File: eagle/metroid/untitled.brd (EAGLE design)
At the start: 100 x 80 mm, 4 parts, among them IC1 MEGA48/88/168-AU, U1 AT45DB321D-S

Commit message: before adding humidity
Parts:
- added C1: 1uF, ng:1206
- added C2, C3, C4, C5, C6: .1uF, ng:1206
- added IC4: MIC5219BM5, metrify:SOT23-5
- added PWR: (no value), con-lstb:MA03-1
- added Q1: (no value), crystal:TC26H
- added S1: (no value), fab:6MM_SWITCH
- added SV1: (no value), con-lstb:MA04-2
- added SV2: (no value), con-lstb:MA08-1
- added U$1: BS-7BATTERYCLIP, metrify:BS-7PACKAGE
- added U$2: DS18S20, metrify:TO92
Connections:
- net N$1 renamed PORTC
- removed net +5V: WRL-00691.1
- removed net AGND: IC1.21
- new net N$1: C6.2, IC1.20
- new net N$10: IC1.27, SV2.5
- new net N$11: IC1.28, SV2.6
- new net N$12: IC1.19, SV2.7
- new net N$13: IC1.22, SV2.8
- new net N$14: IC4.1, IC4.3, PWR.3
- new net N$3: IC1.7, Q1.2
- new net N$4: IC1.8, Q1.1
- new net N$5: IC1.2, U$2.2
- new net N$6: IC1.23, S1.1, S1.2, SV2.1
- new net N$7: IC1.24, SV2.2
- new net N$8: IC1.25, SV2.3
- new net N$9: IC1.26, SV2.4
- net +3V3: now also C1.2, C2.2, C3.2, C4.2, C5.2, IC1.18, IC4.5, PWR.2, SV1.7, U$1.POS, U$2.1, WRL-00691.1
- net GND: now also C1.1, C2.1, C3.1, C4.1, C5.1, C6.1, IC1.21, IC4.2, PWR.1, S1.3, S1.4, SV1.8, U$1.NEG, U$2.3
- net MISO: now also SV1.2
- net MOSI: now also SV1.3
- net RFCEN: now also SV1.6
- net RFIRQ: now also SV1.1
- net RFSPICS: now also SV1.5
- net SCK: now also SV1.4

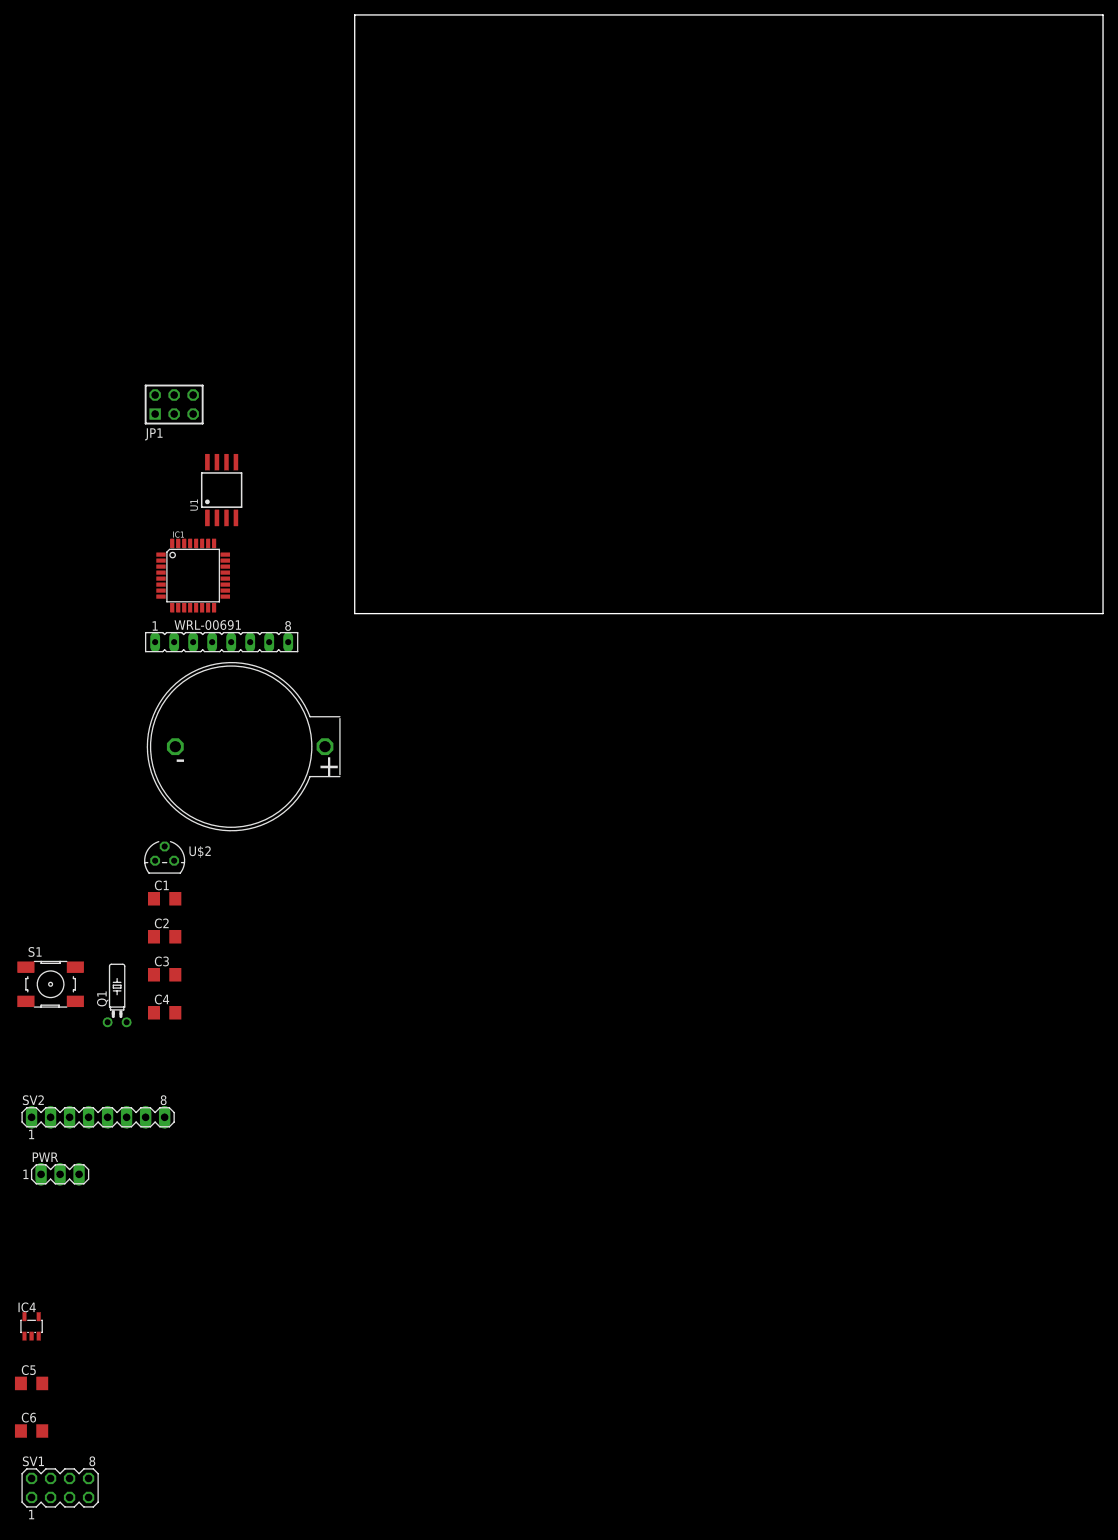
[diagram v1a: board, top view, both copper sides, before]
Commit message: board routed. eagle 6. 6 mil traces, qfp atmega+battery+labpowerheaders+headers>sparkfunnordic or mdfly+pads for 1206 sensors, humidity, phototransistor+isp+pushbutton
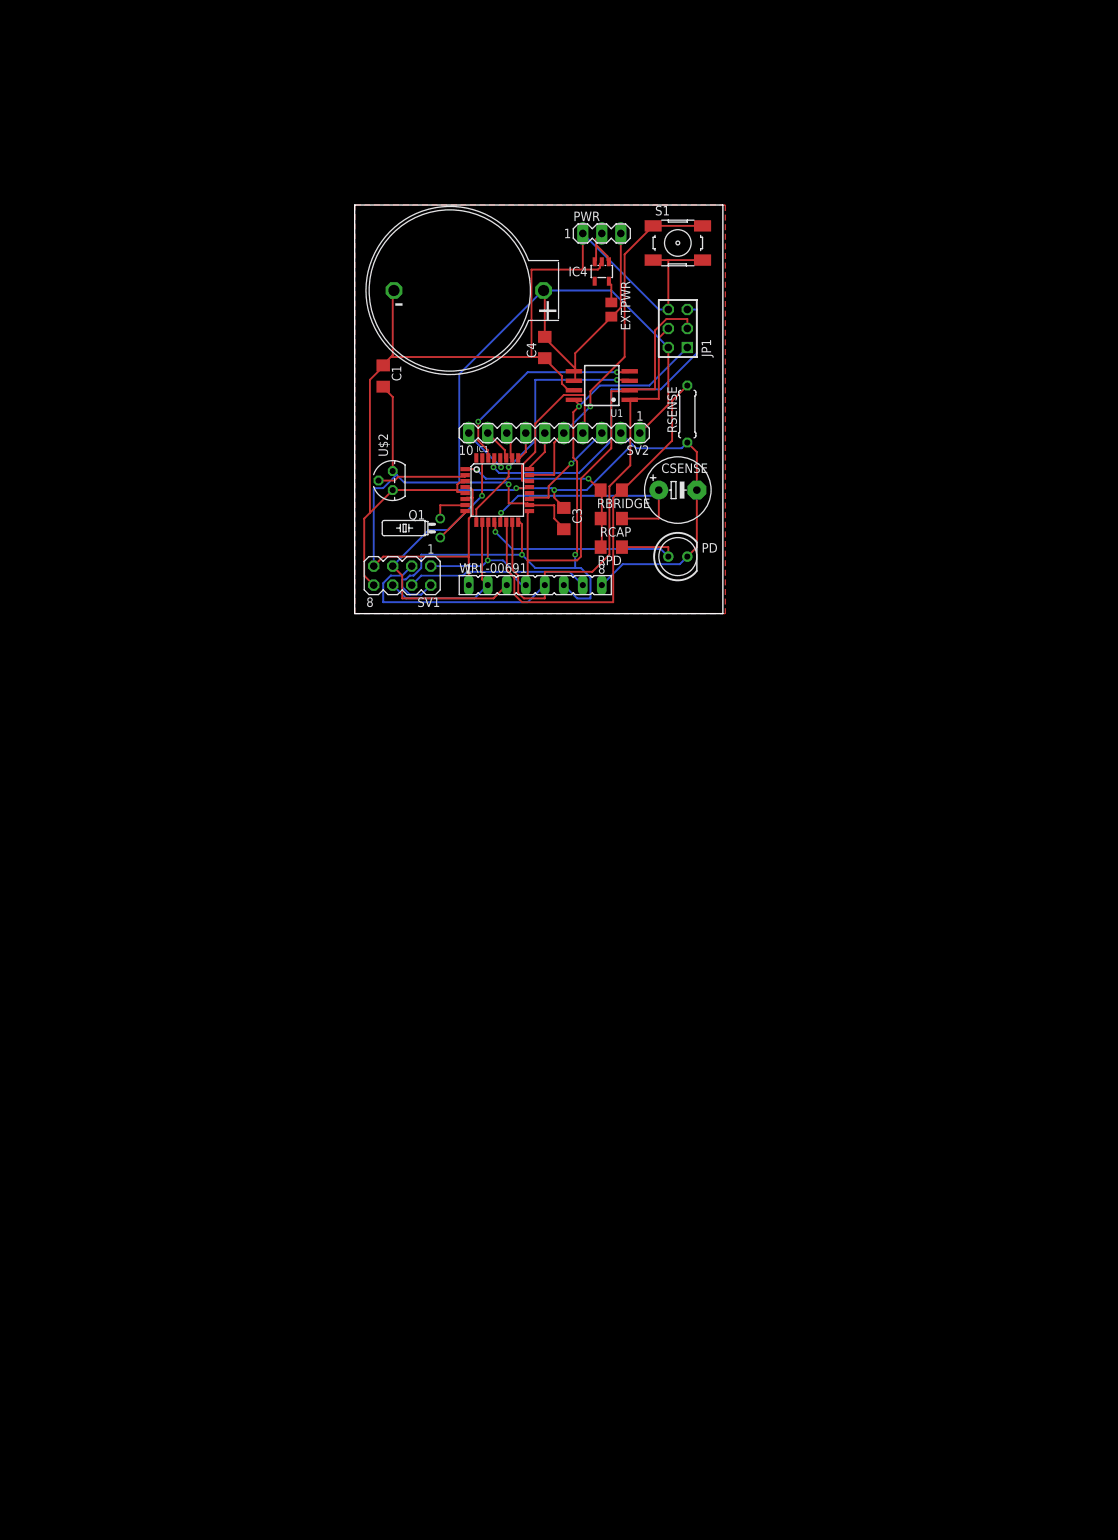
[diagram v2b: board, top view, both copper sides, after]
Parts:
- removed C2, C5, C6: .1uF, ng:1206
- added CSENSE: (no value), rcl:E5-8,5
- added EXTPWR: (no value), rcl:M0805
- added PD: (no value), ng:5MM
- added RBRIDGE, RCAP, RPD: (no value), ng:1206
- added RSENSE: (no value), rcl:0207/7
- JP1: value AVR-ISP-6VERT -> AVR-ISP
- SV1: value (none) -> RF-IS2411
- SV2: value (none) -> ADC; device con-lstb:MA08-1 -> con-lstb:MA10-1
- moved IC4 160.2 mm to (33.0, 45.7), turned to 180 degrees
- moved PWR 145.1 mm to (33.0, 50.8)
- moved SV1 130.2 mm to (6.35, 5.08), turned to 180 degrees
- moved S1 129.8 mm to (43.2, 49.5)
- moved SV2 109.9 mm to (26.7, 24.1), turned to 180 degrees
- moved C4 102.4 mm to (25.4, 35.6), turned to 90 degrees
- moved C3 81.0 mm to (27.9, 12.7), turned to 270 degrees
- moved Q1 78.9 mm to (11.4, 11.4), turned to 90 degrees
- moved C1 75.7 mm to (3.81, 31.8), turned to 270 degrees
- moved JP1 68.1 mm to (43.2, 38.1), turned to 90 degrees
- moved U$1 67.6 mm to (15.2, 43.2)
- moved U$2 59.2 mm to (5.08, 17.8), turned to 90 degrees
- moved U1 52.7 mm to (33.0, 30.5), turned to 90 degrees
- moved WRL-00691 42.6 mm to (24.1, 3.81)
- moved IC1 42.2 mm to (19.1, 16.5)
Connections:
- net N$5 renamed 1WIRE
- removed net N$1: C6.2, IC1.20
- removed net N$7: IC1.24, SV2.2
- new net AUXSENSE: IC1.1, RBRIDGE.2, RCAP.2, RPD.2
- new net HUMIDITY: CSENSE.+, IC1.13, RCAP.1
- new net N$15: IC1.19, SV2.3
- new net N$5: EXTPWR.1, IC4.5
- new net PHOTODIODE: IC1.12, PD.IN, RPD.1
- new net RBRIDGE: IC1.14, RBRIDGE.1, RSENSE.2
- net +3V3: now also EXTPWR.2, PWR.3, SV2.1; no longer C2.2, C5.2, IC4.5, PWR.2
- net GND: now also CSENSE.-, PD.OUT, RSENSE.1, SV2.2; no longer C2.1, C5.1, C6.1
- net N$10: now also IC1.26, SV2.8; no longer IC1.27, SV2.5
- net N$11: now also IC1.27, SV2.9; no longer IC1.28, SV2.6
- net N$12: now also IC1.28, SV2.10; no longer IC1.19, SV2.7
- net N$13: now also SV2.4; no longer SV2.8
- net N$14: now also PWR.2; no longer PWR.3
- net N$6: now also SV2.5; no longer SV2.1
- net N$8: now also IC1.24, SV2.6; no longer IC1.25, SV2.3
- net N$9: now also IC1.25, SV2.7; no longer IC1.26, SV2.4
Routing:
- net GND: track 0.00 -> 219.7 mm, vias 0 -> 2
- net +3V3: track 0.00 -> 181.0 mm, vias 0 -> 1
- net MOSI: track 0.00 -> 92.4 mm
- net MISO: track 0.00 -> 87.5 mm, vias 0 -> 3
- net SCK: track 0.00 -> 78.0 mm
- net RBRIDGE: track 0.00 -> 57.0 mm
- net N$6: track 0.00 -> 48.7 mm, vias 0 -> 1
- net RESET: track 0.00 -> 46.5 mm, vias 0 -> 1
- net RFSPICS: track 0.00 -> 40.4 mm, vias 0 -> 1
- net N$2: track 0.00 -> 34.9 mm, vias 0 -> 2
- net PHOTODIODE: track 0.00 -> 33.4 mm, vias 0 -> 1
- net HUMIDITY: track 0.00 -> 32.4 mm, vias 0 -> 1
- net PORTC: track 0.00 -> 28.4 mm, vias 0 -> 2
- net AUXSENSE: track 0.00 -> 27.3 mm, vias 0 -> 2
- net RFIRQ: track 0.00 -> 27.2 mm, vias 0 -> 1
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- added copper zone on layer 1, net GND
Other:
- board size 100 x 80 mm -> 49.2 x 54.6 mm
- board text added: "-"
- board text added: "3v"
- board text added: "A0"
- board text added: "A1"
- board text added: "A2"
- board text added: "A3"
- board text added: "A4"
- board text added: "A5"
- board text added: "A6"
- board text added: "A7"

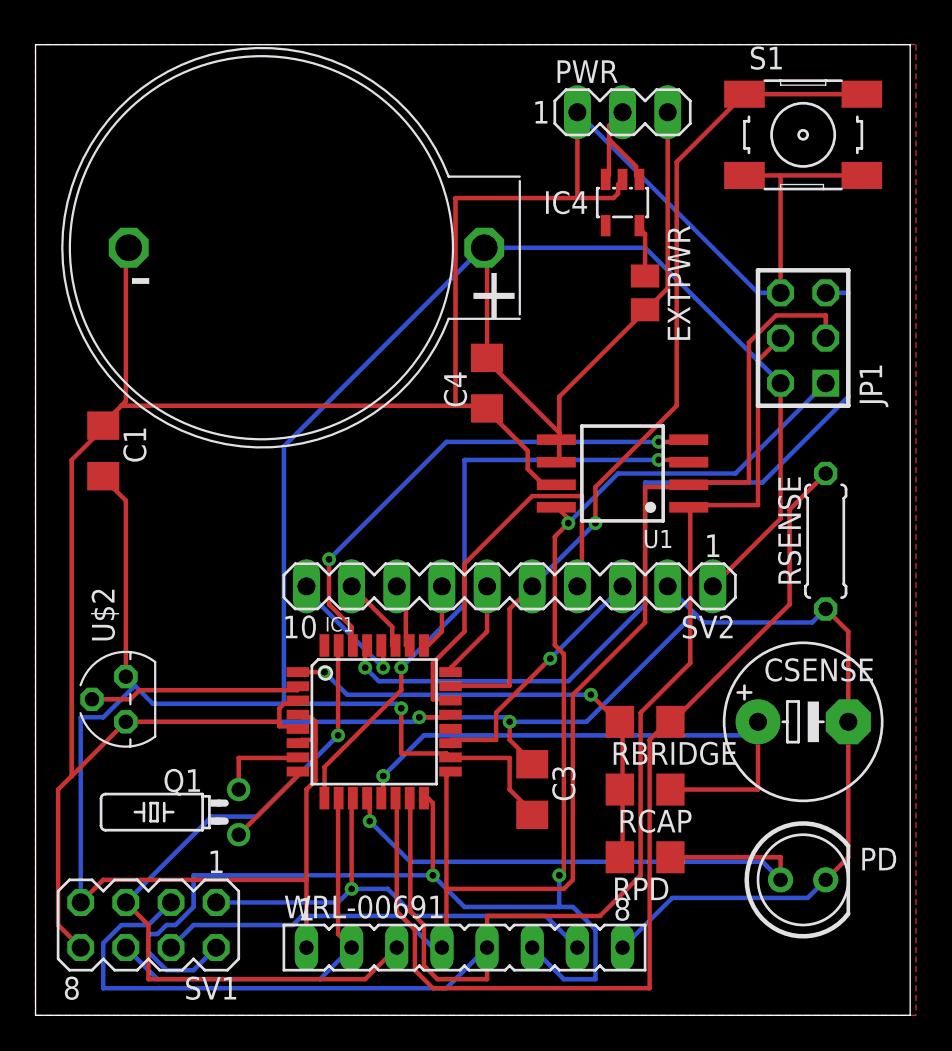
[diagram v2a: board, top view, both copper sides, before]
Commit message: ordered barebones boards from 4pcb, added sch screenshot
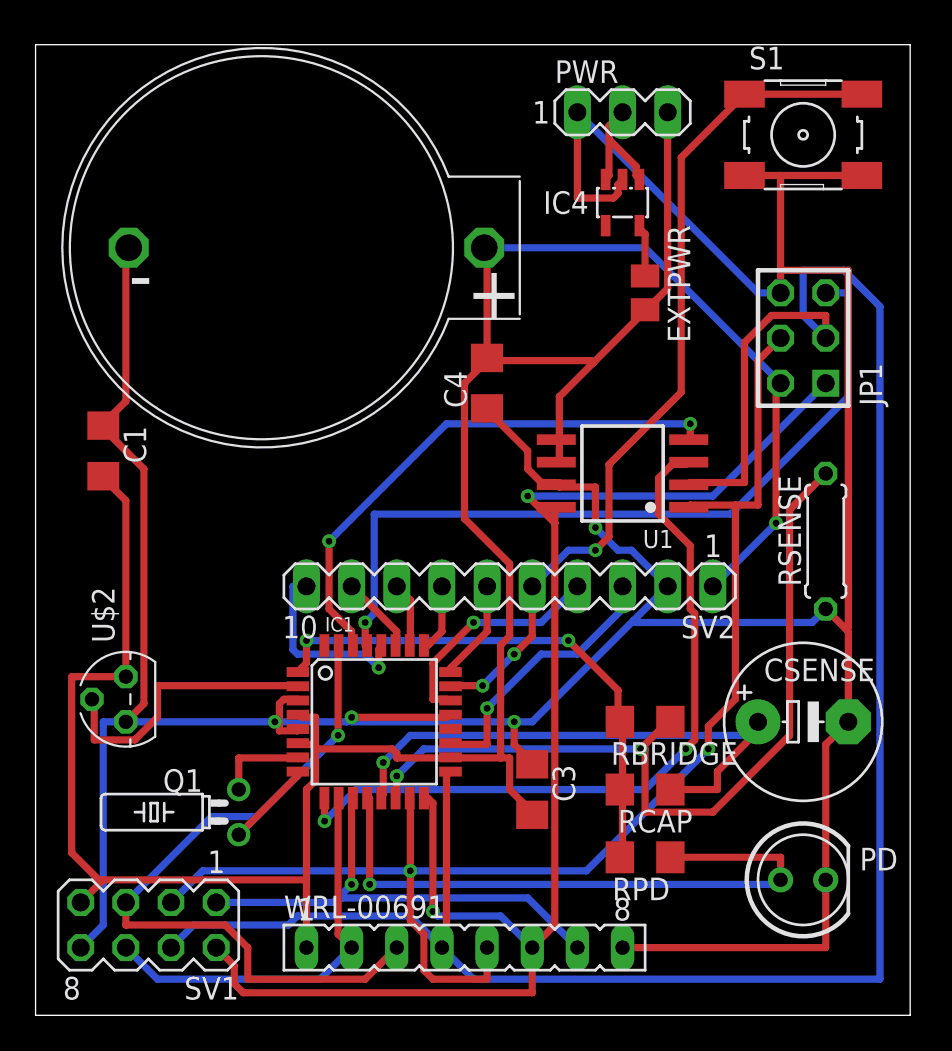
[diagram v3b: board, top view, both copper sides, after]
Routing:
- net SCK: track 78.0 -> 117.1 mm
- net +3V3: track 181.0 -> 162.6 mm
- net MOSI: track 92.4 -> 77.6 mm, vias 0 -> 2
- net N$13: track 22.7 -> 12.9 mm, vias 0 -> 1
- net RBRIDGE: track 57.0 -> 47.2 mm, vias 0 -> 2
- net GND: track 219.7 -> 210.0 mm, vias 2 -> 4
- net N$2: track 34.9 -> 41.6 mm
- net MISO: track 87.5 -> 82.0 mm, vias 3 -> 2
- net 1WIRE: track 12.0 -> 16.2 mm
- net AUXSENSE: track 27.3 -> 30.6 mm
- net N$12: track 7.63 -> 10.9 mm
- net RESET: track 46.5 -> 44.2 mm
- net PHOTODIODE: track 33.4 -> 35.7 mm
- net PORTC: track 28.4 -> 30.4 mm
- net N$15: track 14.3 -> 15.3 mm
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- removed copper zone on layer 1, net GND
